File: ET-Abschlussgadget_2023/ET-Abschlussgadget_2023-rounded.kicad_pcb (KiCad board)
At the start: 2 copper layers, 85 x 54 mm, 37 parts, among them J1 PB0, J2 PB1, J3 UPDI / RESET, J4 EXTCLK, J5 EXTCLK, J6 EXTCLK, SW1 ON/OFF, U1 ATtiny414-SS

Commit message: Removed all designators, add silkscreen below MCU and LEDs
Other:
- board text added: "ATtiny414"

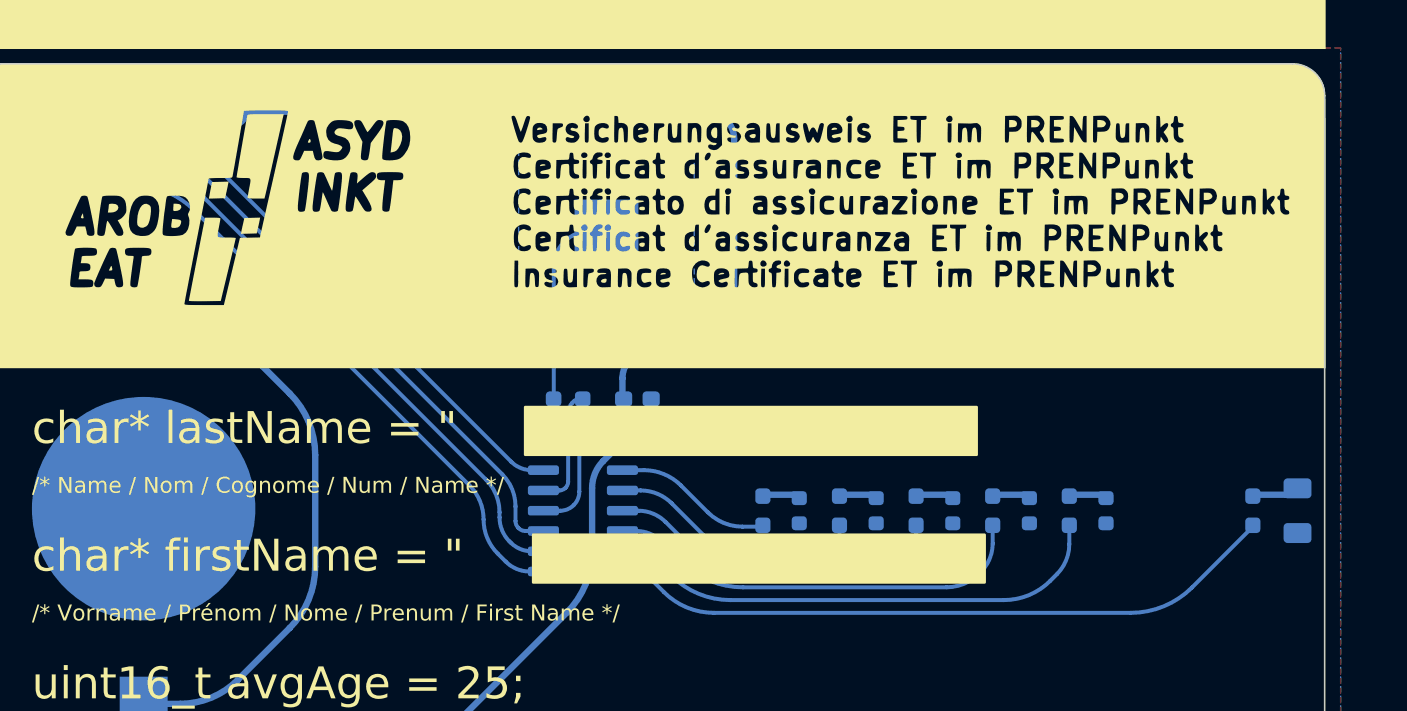
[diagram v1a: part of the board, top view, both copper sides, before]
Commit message: Add ground plane pattern to entire back side
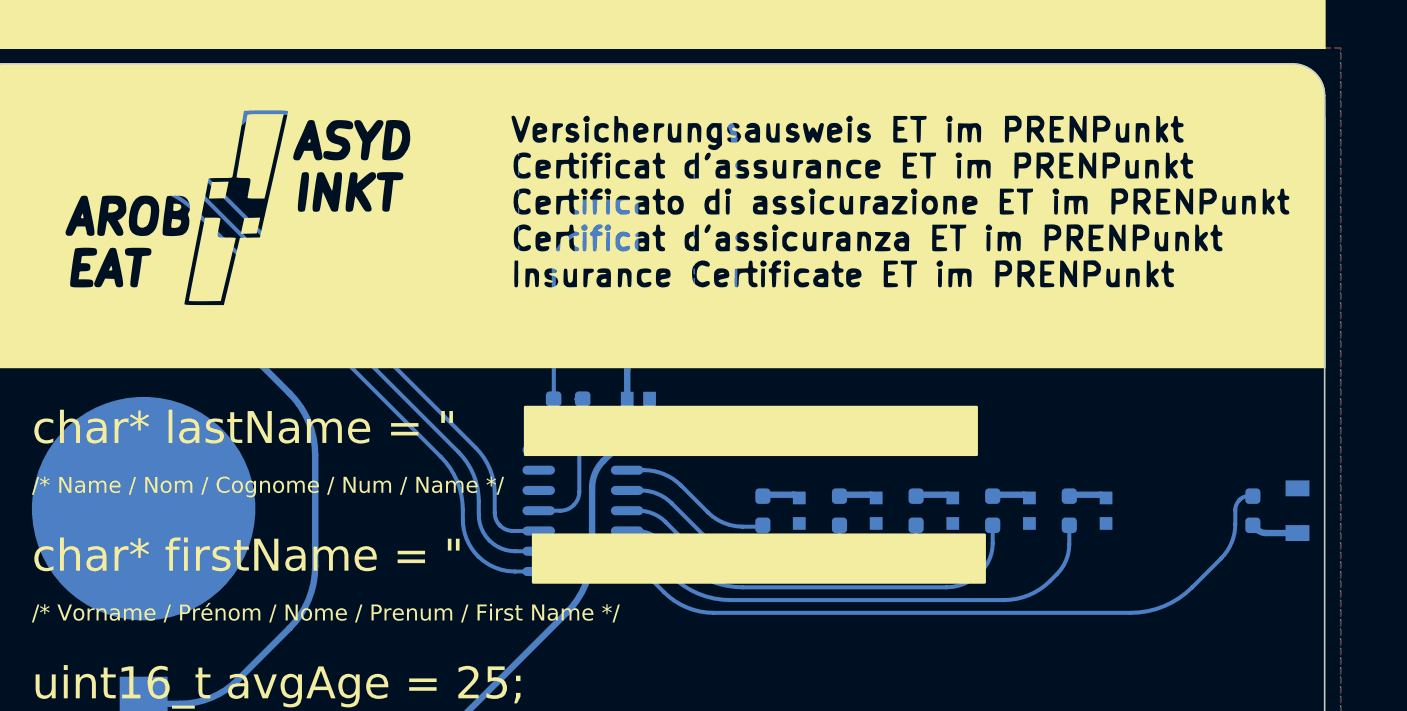
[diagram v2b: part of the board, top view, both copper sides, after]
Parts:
- removed J4: EXTCLK, TestPoint:TestPoint_Pad_D2.0mm
- C1: footprint Capacitor_SMD:C_0603_1608Metric_Pad1.08x0.95mm_HandSolder -> easyeda2kicad:C0603
- D1: footprint LED_SMD:LED_1206_3216Metric -> easyeda2kicad:LED-SMD_L3.2-W2.1-R-FD
- D2, D3, D4, D5, D6: footprint LED_SMD:LED_0603_1608Metric -> easyeda2kicad:LED0603-RD_RED
- R5: value 590 -> 220
- U1: footprint Package_SO:SOIC-14_3.9x8.7mm_P1.27mm -> easyeda2kicad:SOIC-14_L8.7-W3.9-P1.27-LS6.0-BL
- moved G*** 71.3 mm to (213.9, 79.6)
- moved G*** 70.1 mm to (160.0, 122.0)
- moved J3 2.54 mm to (111.5, 83.0)
- moved C1 0.06 mm to (142.0, 101.0)
- turned R1 to 90 degrees
- turned U1 to -90 degrees
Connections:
- U1 pad 12: /Cap_Pad / ADC1 -> unconnected-(U1-PA2-Pad12)
- U1 pad 13: /EXTCLK -> unconnected-(U1-PA3-Pad13)
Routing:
- net /EXTCLK: track 34.2 -> 0.00 mm
- net /Cap_Pad / ADC1: track 16.2 -> 9.05 mm
- net /LED IR: track 42.3 -> 44.3 mm
- net /UPDI / RESET: track 39.4 -> 37.5 mm
- net Net-(J2-Pin_1): track 46.0 -> 46.7 mm
- net Net-(J1-Pin_1): track 43.5 -> 44.1 mm

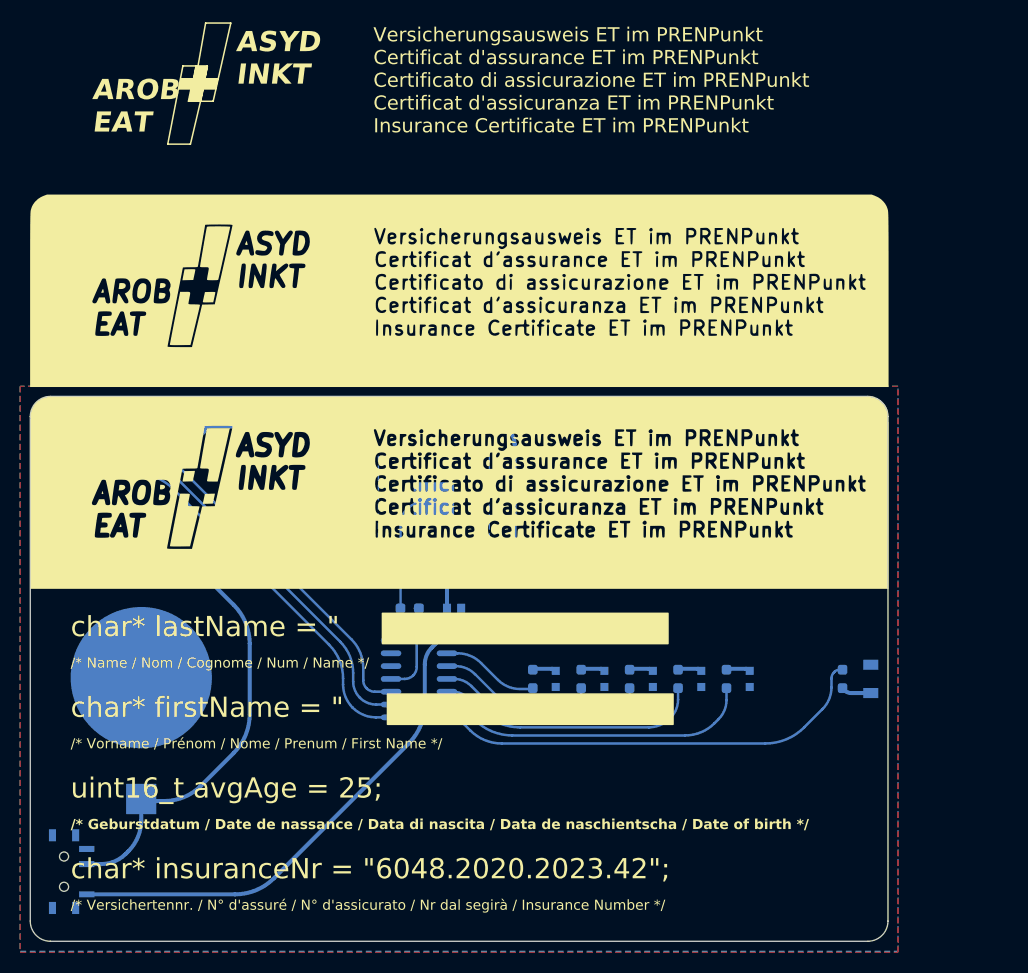
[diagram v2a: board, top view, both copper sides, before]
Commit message: Remove pulldown, Update resistors, Update routing
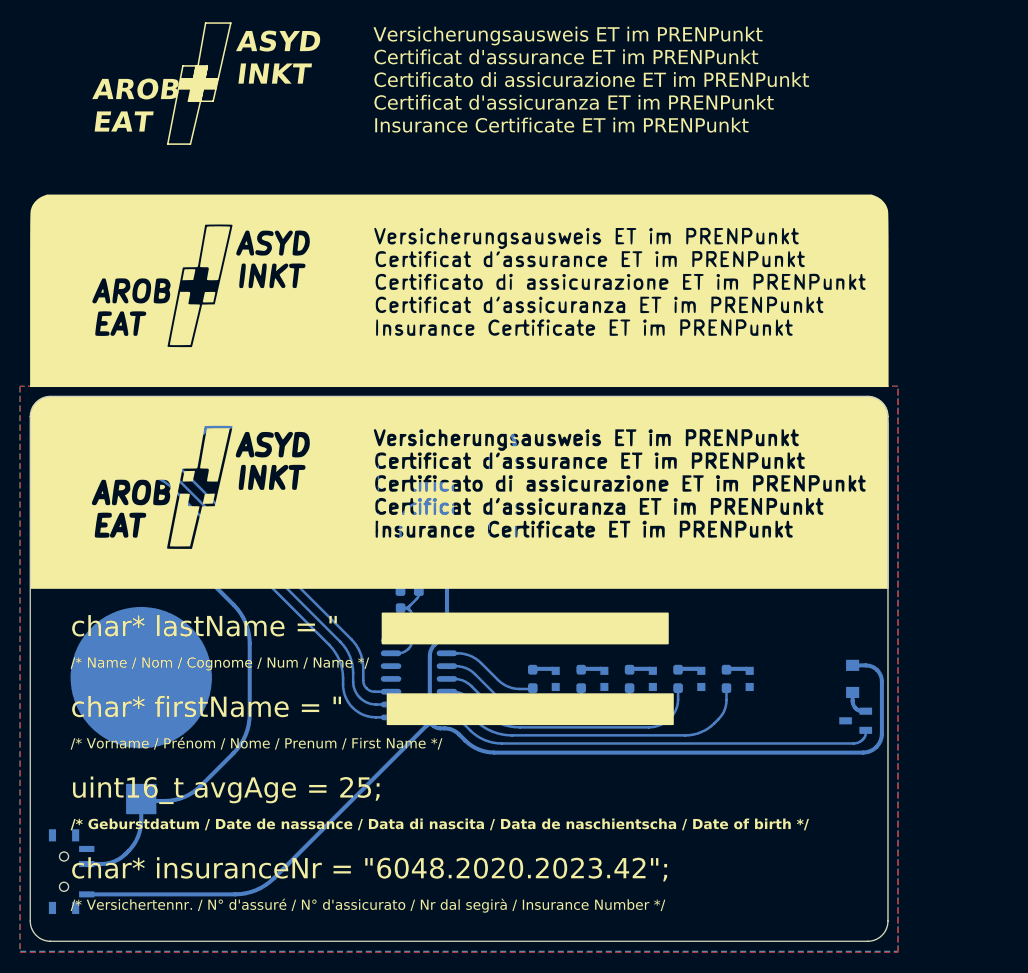
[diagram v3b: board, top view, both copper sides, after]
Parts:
- removed R1: 590, Resistor_SMD:R_0603_1608Metric_Pad0.98x0.95mm_HandSolder
- added Q1: NMOS, easyeda2kicad:SOT-23-3_L2.9-W1.3-P1.90-LS2.4-BR, B.Cu at (181.8, 112.2)
- added R8: 1M, Resistor_SMD:R_0603_1608Metric_Pad0.98x0.95mm_HandSolder, B.Cu at (136.7, 101.9)
- D1: footprint easyeda2kicad:LED-SMD_L3.2-W2.1-R-FD -> Diode_SMD:XS-IR04A05-802
- R2, R3, R4, R6, R7: value 590 -> 560
- R5: value 220 -> 560
- moved D1 1.80 mm to (181.5, 108.0)
- moved R5 1.70 mm to (137.6, 99.3)
- moved C1 1.00 mm to (142.0, 102.0)
- renumbered J5 to J1, J6 to J2, J1 to J3, J2 to J4, J3 to J5
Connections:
- D1 pad 1: GND -> Net-(D1-K)
- D1 pad 2: Net-(D1-A) -> VCC
- U1 pad 11: /Cap_Pad / ADC1 -> unconnected-(U1-PA1-Pad11)
- U1 pad 13: unconnected-(U1-PA3-Pad13) -> /Cap_Pad / ADC1
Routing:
- net VCC: track 106.3 -> 163.3 mm
- net Net-(D1-A): track 2.96 -> 0.00 mm
- net Net-(D1-K): track 0.00 -> 2.72 mm
- net /Cap_Pad: track 12.8 -> 11.1 mm
- net /LED IR: track 44.3 -> 43.4 mm
- net /Cap_Pad / ADC1: track 9.05 -> 9.74 mm

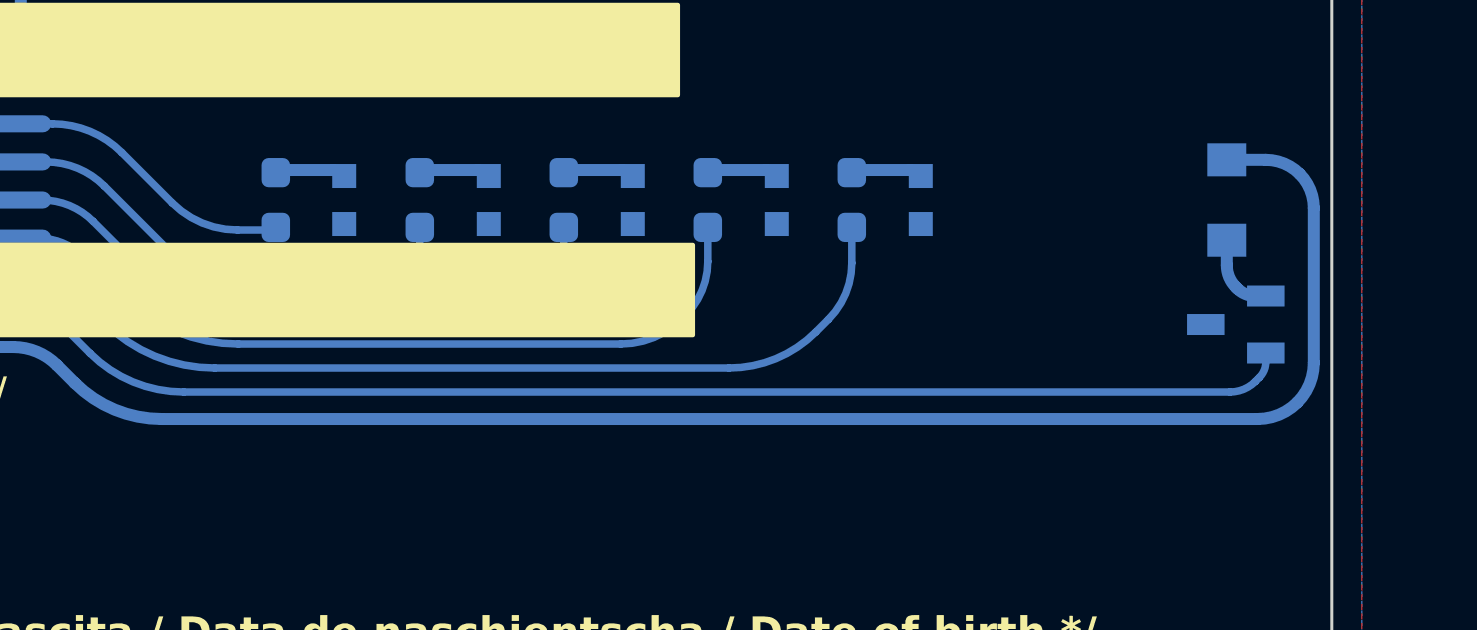
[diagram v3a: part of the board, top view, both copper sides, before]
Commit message: Replaced parts in materialliste, replaced some footprints, generade production-files with JLC-plugin
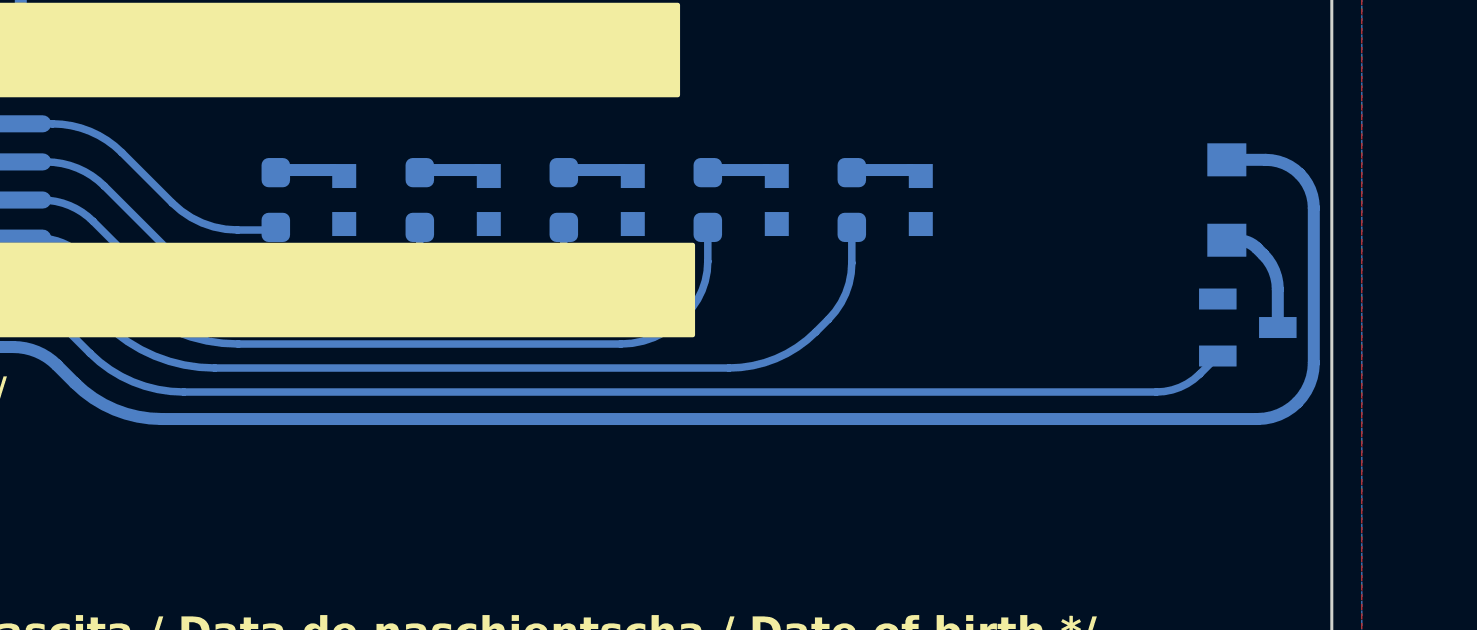
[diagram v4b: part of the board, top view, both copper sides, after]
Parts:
- removed Q1: NMOS, easyeda2kicad:SOT-23-3_L2.9-W1.3-P1.90-LS2.4-BR
- added Q2: SI2302_C2891732, easyeda2kicad:SOT-23-3_L2.9-W1.3-P1.90-LS2.4-BR, B.Cu at (182.2, 112.2)
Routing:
- net /LED IR: track 43.4 -> 41.4 mm
- net Net-(D1-K): track 2.72 -> 3.93 mm
